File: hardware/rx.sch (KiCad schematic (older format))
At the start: 18 parts, among them J4 SMA, U22 TRF37A73, U23 SKY65404

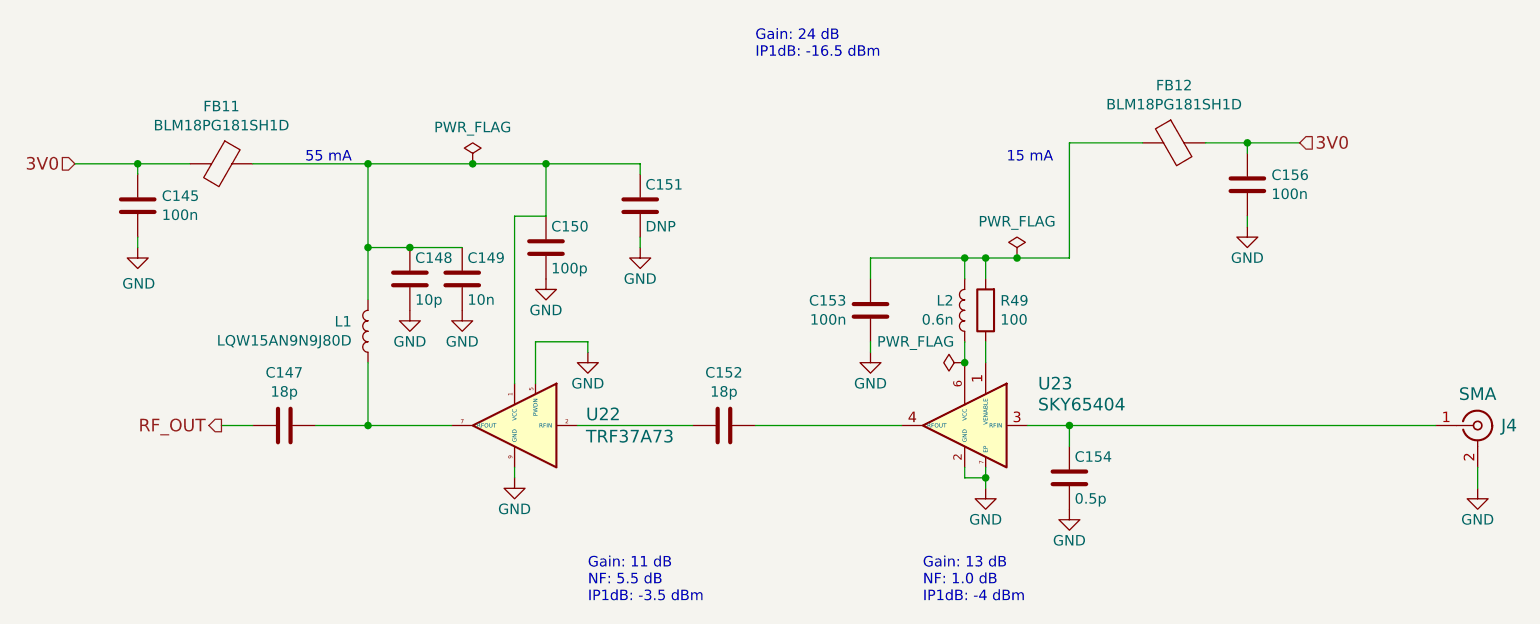
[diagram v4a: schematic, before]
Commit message: Add buffer amp for power amp reference voltage.
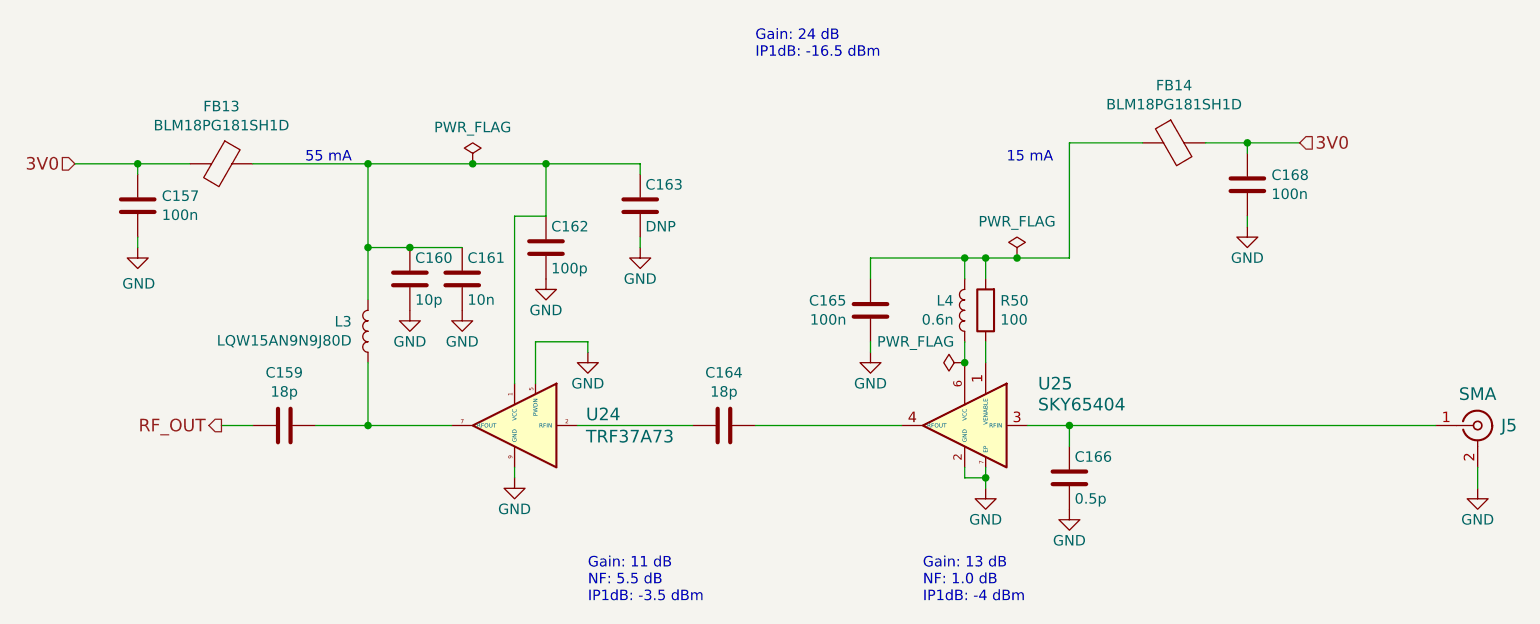
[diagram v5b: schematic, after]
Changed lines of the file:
@@
 EESchema Schematic File Version 4
 LIBS:fmcw-cache
-EELAYER 29 0
+EELAYER 26 0
 EELAYER END
 $Descr A4 11693 8268
@@
 AR Path="/59396B97/593BC199" Ref="U23"  Part="1"
 AR Path="/593D90BA/593BC199" Ref="U25"  Part="1"
-F 0 "U23" H 6550 4150 60  0000 R CNN
+F 0 "U25" H 6550 4150 60  0000 R CNN
 F 1 "SKY65404" H 6550 4050 60  0000 R CNN
 F 2 "Package_DFN_QFN:Skyworks_DFN-6-1EP_1.5x1.5mm_P0.5mm_EP0.7x1.2mm" H 6750 3950 60  0001 C CNN
@@
 AR Path="/59396B97/593BC396" Ref="R49"  Part="1"
 AR Path="/593D90BA/593BC396" Ref="R50"  Part="1"
-F 0 "R49" H 6730 3354 50  0000 R CNN
+F 0 "R50" H 6730 3354 50  0000 R CNN
 F 1 "100" H 6730 3445 50  0000 R CNN
 F 2 "Resistor_SMD:R_0402_1005Metric" V 6730 3400 30  0001 C CNN
@@
 AR Path="/59396B97/593BC695" Ref="L2"  Part="1"
 AR Path="/593D90BA/593BC695" Ref="L4"  Part="1"
-F 0 "L2" H 6753 3354 50  0000 L CNN
+F 0 "L4" H 6753 3354 50  0000 L CNN
 F 1 "0.6n" H 6753 3445 50  0000 L CNN
 F 2 "Inductor_SMD:L_0402_1005Metric" H 6700 3400 60  0001 C CNN
@@
 AR Path="/59396B97/593BC767" Ref="C153"  Part="1"
 AR Path="/593D90BA/593BC767" Ref="C165"  Part="1"
-F 0 "C153" H 6135 3446 50  0000 R CNN
+F 0 "C165" H 6135 3446 50  0000 R CNN
 F 1 "100n" H 6135 3355 50  0000 R CNN
 F 2 "Capacitor_SMD:C_0402_1005Metric" H 6288 3250 30  0001 C CNN
@@
 AR Path="/59396B97/593BCCCA" Ref="J4"  Part="1"
 AR Path="/593D90BA/593BCCCA" Ref="J5"  Part="1"
-F 0 "J4" H 9300 3950 60  0000 C CNN
+F 0 "J5" H 9300 3950 60  0000 C CNN
 F 1 "SMA" H 9150 4100 60  0000 C CNN
 F 2 "fmcw:CONSMA003.062" H 9150 3950 60  0001 C CNN
@@
 AR Path="/59396B97/593BCEBC" Ref="C154"  Part="1"
 AR Path="/593D90BA/593BCEBC" Ref="C166"  Part="1"
-F 0 "C154" H 7225 4300 50  0000 L CNN
+F 0 "C166" H 7225 4300 50  0000 L CNN
 F 1 "0.5p" H 7225 4100 50  0000 L CNN
 F 2 "Capacitor_SMD:C_0402_1005Metric" H 7238 4050 30  0001 C CNN
@@
 AR Path="/59396B97/593BD4EF" Ref="C152"  Part="1"
 AR Path="/593D90BA/593BD4EF" Ref="C164"  Part="1"
-F 0 "C152" V 5298 3950 50  0000 C CNN
+F 0 "C164" V 5298 3950 50  0000 C CNN
 F 1 "18p" V 5389 3950 50  0000 C CNN
 F 2 "Capacitor_SMD:C_0402_1005Metric" H 5588 3800 30  0001 C CNN
@@
 AR Path="/59396B97/593BD8E8" Ref="L1"  Part="1"
 AR Path="/593D90BA/593BD8E8" Ref="L3"  Part="1"
-F 0 "L1" H 3928 3454 50  0000 L CNN
+F 0 "L3" H 3928 3454 50  0000 L CNN
 F 1 "LQW15AN9N9J80D" H 3928 3545 50  0000 L CNN
 F 2 "Inductor_SMD:L_0402_1005Metric" H 3850 3500 60  0001 C CNN
@@
 AR Path="/59396B97/593BDA25" Ref="C148"  Part="1"
 AR Path="/593D90BA/593BDA25" Ref="C160"  Part="1"
-F 0 "C148" H 4075 3350 50  0000 L CNN
+F 0 "C160" H 4075 3350 50  0000 L CNN
 F 1 "10p" H 4075 3150 50  0000 L CNN
 F 2 "Capacitor_SMD:C_0402_1005Metric" H 4088 3100 30  0001 C CNN
@@
 AR Path="/59396B97/593BDF98" Ref="C147"  Part="1"
 AR Path="/593D90BA/593BDF98" Ref="C159"  Part="1"
-F 0 "C147" V 3198 3950 50  0000 C CNN
+F 0 "C159" V 3198 3950 50  0000 C CNN
 F 1 "18p" V 3289 3950 50  0000 C CNN
 F 2 "Capacitor_SMD:C_0402_1005Metric" H 3488 3800 30  0001 C CNN
@@
 AR Path="/593D90BA/59751767" Ref="FB13"  Part="1"
 AR Path="/59396B97/59751767" Ref="FB11"  Part="1"
-F 0 "FB11" V 2876 2700 50  0000 C CNN
+F 0 "FB13" V 2876 2700 50  0000 C CNN
 F 1 "BLM18PG181SH1D" V 2967 2700 50  0000 C CNN
 F 2 "Inductor_SMD:L_0603_1608Metric" H 3150 2700 60  0001 C CNN
@@
 AR Path="/593D90BA/59751D28" Ref="C163"  Part="1"
 AR Path="/59396B97/59751D28" Ref="C151"  Part="1"
-F 0 "C151" H 5175 3000 50  0000 L CNN
+F 0 "C163" H 5175 3000 50  0000 L CNN
 F 1 "DNP" H 5175 2800 50  0000 L CNN
 F 2 "Capacitor_SMD:C_0603_1608Metric" H 5188 2750 30  0001 C CNN
@@
 AR Path="/593D90BA/597527FA" Ref="FB14"  Part="1"
 AR Path="/59396B97/597527FA" Ref="FB12"  Part="1"
-F 0 "FB12" V 7426 2600 50  0000 C CNN
+F 0 "FB14" V 7426 2600 50  0000 C CNN
 F 1 "BLM18PG181SH1D" V 7517 2600 50  0000 C CNN
 F 2 "Inductor_SMD:L_0603_1608Metric" H 7700 2600 60  0001 C CNN
@@
 AR Path="/593D90BA/597605DF" Ref="U24"  Part="1"
 AR Path="/597605DF" Ref="U?"  Part="1"
-F 0 "U22" H 4409 4003 60  0000 R CNN
+F 0 "U24" H 4409 4003 60  0000 R CNN
 F 1 "TRF37A73" H 4409 3897 60  0000 R CNN
 F 2 "Package_SON:WSON-8-1EP_2x2mm_P0.5mm_EP0.9x1.6mm" H 4450 3900 60  0001 C CNN
@@
 AR Path="/59396B97/59761DBE" Ref="C150"  Part="1"
 AR Path="/593D90BA/59761DBE" Ref="C162"  Part="1"
-F 0 "C150" H 4725 3200 50  0000 L CNN
+F 0 "C162" H 4725 3200 50  0000 L CNN
 F 1 "100p" H 4725 3000 50  0000 L CNN
 F 2 "Capacitor_SMD:C_0402_1005Metric" H 4738 2950 30  0001 C CNN
@@
 AR Path="/59396B97/59762FC5" Ref="C149"  Part="1"
 AR Path="/593D90BA/59762FC5" Ref="C161"  Part="1"
-F 0 "C149" H 4325 3350 50  0000 L CNN
+F 0 "C161" H 4325 3350 50  0000 L CNN
 F 1 "10n" H 4325 3150 50  0000 L CNN
 F 2 "Capacitor_SMD:C_0402_1005Metric" H 4338 3100 30  0001 C CNN
@@
 AR Path="/59396B97/5C42C3BD" Ref="C156"  Part="1"
 AR Path="/593D90BA/5C42C3BD" Ref="C168"  Part="1"
-F 0 "C156" H 8165 2846 50  0000 L CNN
+F 0 "C168" H 8165 2846 50  0000 L CNN
 F 1 "100n" H 8165 2755 50  0000 L CNN
 F 2 "Capacitor_SMD:C_0402_1005Metric" H 8088 2650 30  0001 C CNN
@@
 AR Path="/59396B97/5C42DC20" Ref="C145"  Part="1"
 AR Path="/593D90BA/5C42DC20" Ref="C157"  Part="1"
-F 0 "C145" H 2865 2946 50  0000 L CNN
+F 0 "C157" H 2865 2946 50  0000 L CNN
 F 1 "100n" H 2865 2855 50  0000 L CNN
 F 2 "Capacitor_SMD:C_0402_1005Metric" H 2788 2750 30  0001 C CNN
